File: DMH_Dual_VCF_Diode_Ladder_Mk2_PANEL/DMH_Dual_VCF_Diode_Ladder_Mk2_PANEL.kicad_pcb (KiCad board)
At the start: 2 copper layers, 150 x 200 mm, 45 parts, among them J0 Panel_GND_Solder_Wire_Pad

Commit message: Added CV3 and Drive CV to Panel
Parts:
- added H45: Drv CV Amt, SynthStuff:Pot_Cutout_Tiny_attv_P110KH1, F.Cu at (62.8, 166.0)
- added H46: Drv CV Amt, SynthStuff:Pot_Cutout_Tiny_attv_P110KH1, F.Cu at (137.2, 166.0)
- added H47: CV 3, SynthStuff:Jack_6.35mm_Cutout_v3, F.Cu at (66.5, 190.2)
- added H48: Drive CV, SynthStuff:Jack_6.35mm_Cutout_v3, F.Cu at (66.5, 208.8)
- added H49: CV 3, SynthStuff:Jack_6.35mm_Cutout_v3, F.Cu at (133.5, 190.2)
- added H50: Drive CV, SynthStuff:Jack_6.35mm_Cutout_v3, F.Cu at (133.5, 208.8)
- H19, H23: value Bus CV -> Amt
- H33: value Link -> Link CV
- H44: value Feed -> Link D&R
- moved H17 13.0 mm to (38.0, 166.0)
- moved H28 13.0 mm to (162.0, 166.0)
- moved H15 8.33 mm to (150.0, 190.2)
- moved H18 8.33 mm to (50.0, 208.8)
- moved H25 8.33 mm to (150.0, 208.8)
- moved H6 8.33 mm to (50.0, 190.2)
- moved H13 4.50 mm to (87.5, 166.0)
- moved H32 4.50 mm to (112.5, 166.0)
- moved H16 4.00 mm to (166.5, 190.2)
- moved H30 4.00 mm to (166.5, 208.8)
- moved H5 4.00 mm to (33.5, 190.2)
- moved H8 4.00 mm to (33.5, 208.8)
- moved H19 3.83 mm to (83.0, 190.2)
- moved H23 3.83 mm to (117.0, 190.2)
- moved H29 3.83 mm to (117.0, 208.8)
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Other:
- board text removed: "OFF"

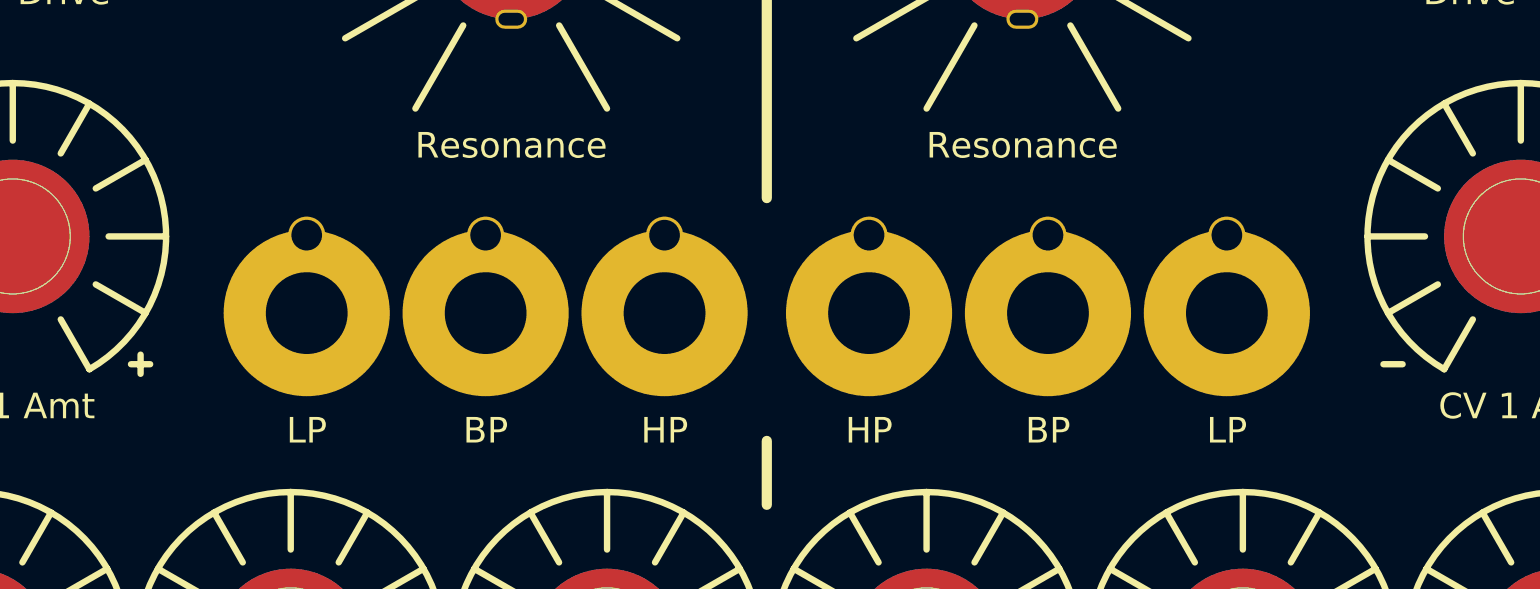
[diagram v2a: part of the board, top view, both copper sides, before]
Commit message: Moved Res Int and CV3 V/Oct trims to front panel
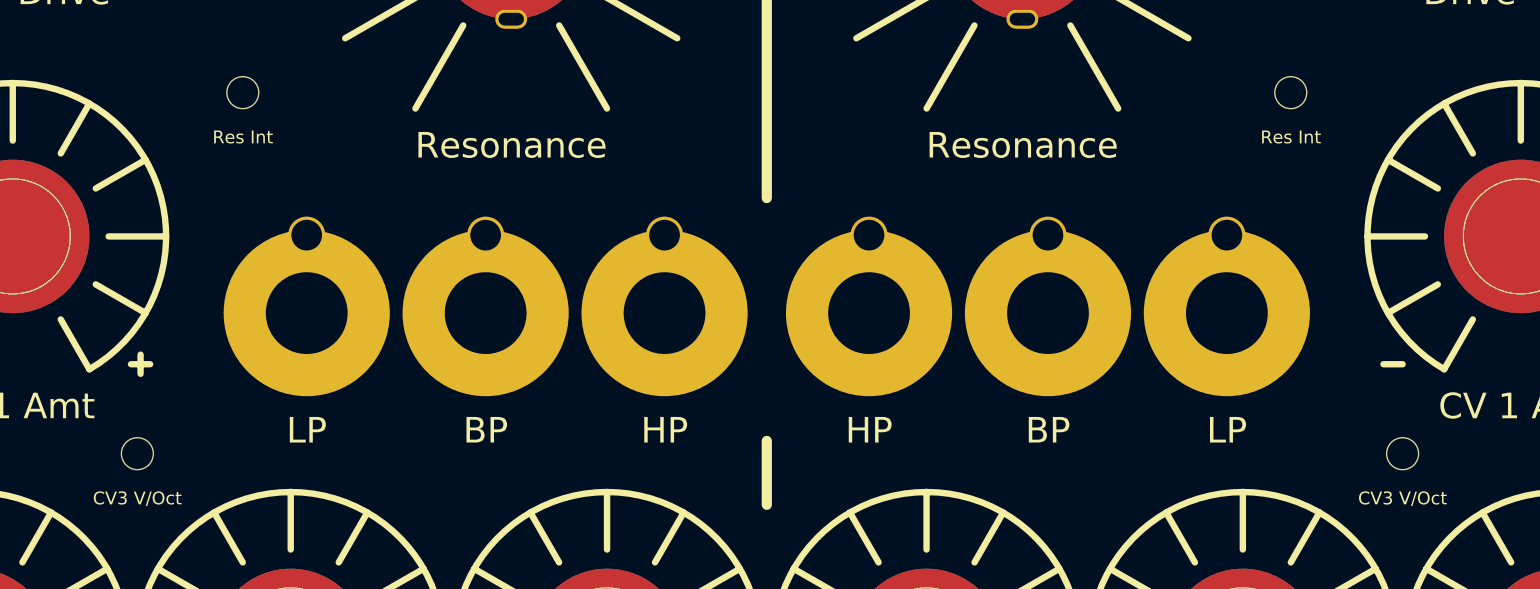
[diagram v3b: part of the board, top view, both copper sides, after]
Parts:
- added H51: Res Int, SynthStuff:MountingHole_TrimPot, F.Cu at (59.0, 122.8)
- added H52: Res Int, SynthStuff:MountingHole_TrimPot, F.Cu at (141.0, 122.8)
- added H53: CV3 V/Oct, SynthStuff:MountingHole_TrimPot, F.Cu at (50.8, 151.0)
- added H54: CV3 V/Oct, SynthStuff:MountingHole_TrimPot, F.Cu at (149.8, 151.0)

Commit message: Finished Mk2.0
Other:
- board text added: "Mk2.0 - March 2025"
- board text removed: "Mk1.0 - Month Year"
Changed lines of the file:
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@@
 		)
 	)
-	(gr_text "Mk1.0 - Month Year"
+	(gr_text "Mk2.0 - March 2025"
 		(at 100 223 0)
 		(layer "B.SilkS")
